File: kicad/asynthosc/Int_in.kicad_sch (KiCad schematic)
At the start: 7 parts, among them J7 AudioJack3, Q1 Q_NPN_BEC, SW2 SW_MEC_5G_LED

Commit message: bom: add jlcpcb field with simplified footprint
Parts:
- C33: JLC (none) -> 0603
- Q1: JLC (none) -> SOT-23
- R24, R25, R26: JLC (none) -> 0402
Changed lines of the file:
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@@
+			)
+		)
+		(property "JLC" ""
+			(at 118.11 60.96 0)
+			(effects
+				(font
+					(size 1.27 1.27)
+				)
+				(hide yes)
 			)
 		)
@@
 			)
 		)
+		(property "JLC" ""
+			(at 50.8 68.58 0)
+			(effects
+				(font
+					(size 1.27 1.27)
+				)
+				(hide yes)
+			)
+		)
 		(pin "S"
 		)
@@
 		)
 		(property "RefNum" "_generic_"
+			(at 71.12 66.04 0)
+			(effects
+				(font
+					(size 1.27 1.27)
+				)
+				(hide yes)
+			)
+		)
+		(property "JLC" "0402"
 			(at 71.12 66.04 0)
 			(effects
@@
 			)
 		)
+		(property "JLC" "0402"
+			(at 102.87 64.77 0)
+			(effects
+				(font
+					(size 1.27 1.27)
+				)
+				(hide yes)
+			)
+		)
 		(pin "1"
 		)
@@
 			)
 		)
+		(property "JLC" "0603"
+			(at 104.14 44.45 0)
+			(effects
+				(font
+					(size 1.27 1.27)
+				)
+				(hide yes)
+			)
+		)
 		(pin "2"
 		)
@@
 			)
 		)
+		(property "JLC" "SOT-23"
+			(at 82.55 66.04 0)
+			(effects
+				(font
+					(size 1.27 1.27)
+				)
+				(hide yes)
+			)
+		)
 		(pin "1"
 		)
@@
 			(at 85.09 53.34 0)
 			(effects
+				(font
+					(size 1.27 1.27)
+				)
+				(hide yes)
+			)
+		)
+		(property "JLC" "0402"
+			(at 85.09 53.34 0)
+			(effects

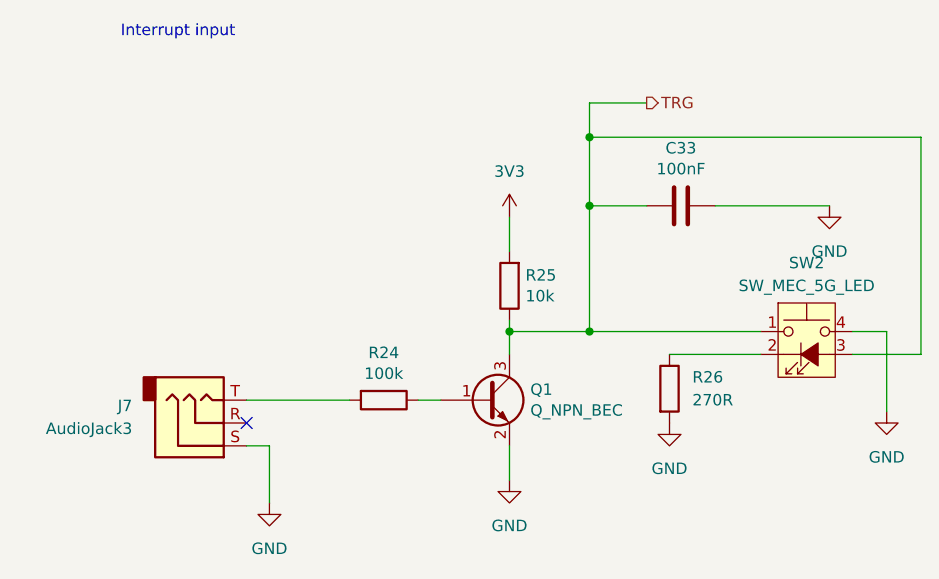
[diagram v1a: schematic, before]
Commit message: bom: dnp for all manually equiped components
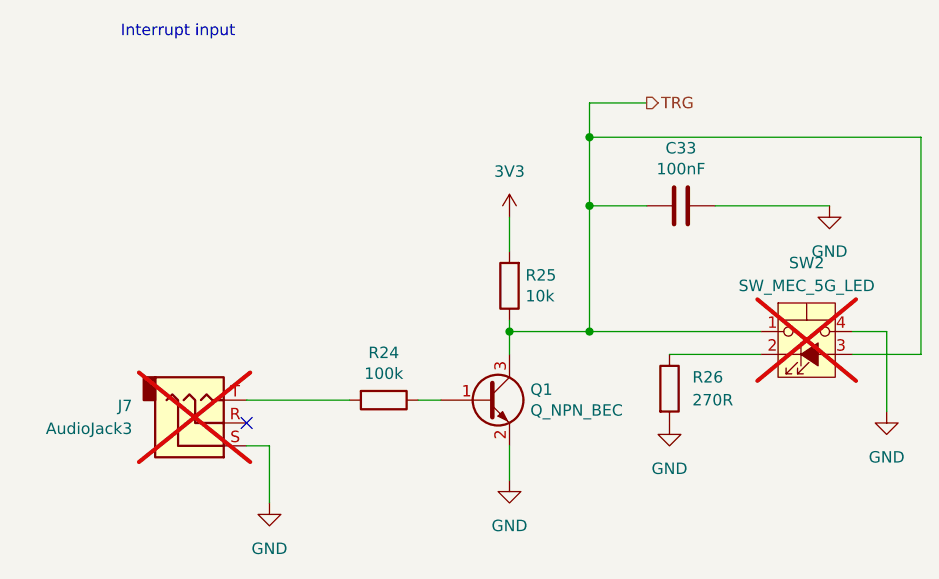
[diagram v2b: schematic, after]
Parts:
- J7, SW2: now not fitted
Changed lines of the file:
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@@
 		(in_bom yes)
 		(on_board yes)
-		(dnp no)
+		(dnp yes)
 		(fields_autoplaced yes)
 		(property "Reference" "SW2"
@@
 		(in_bom yes)
 		(on_board yes)
-		(dnp no)
+		(dnp yes)
 		(property "Reference" "J7"
 			(at 43.18 66.6749 0)

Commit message: bom: adding jlc ref to generic
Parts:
- C33: LCSC (none) -> C14663
- R24: LCSC (none) -> C25741
- R25: LCSC (none) -> C25744
- R26: LCSC (none) -> C144055
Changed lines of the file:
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@@
 			)
 		)
-		(property "LCSC" ""
+		(property "LCSC" "C25741"
 			(at 71.12 66.04 0)
 			(effects
@@
 			)
 		)
-		(property "LCSC" ""
+		(property "LCSC" "C144055"
 			(at 102.87 64.77 0)
 			(effects
@@
 			)
 		)
-		(property "LCSC" ""
+		(property "LCSC" "C14663"
 			(at 104.14 44.45 0)
 			(effects
@@
 			)
 		)
-		(property "LCSC" ""
+		(property "LCSC" "C25744"
 			(at 85.09 53.34 0)
 			(effects

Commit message: sch: update to k9 libs, fix nets
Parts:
- Q1: symbol Device:Q_NPN_BEC -> Transistor_BJT:Q_NPN_BEC
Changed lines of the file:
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@@
 	)
 	(symbol
-		(lib_id "Device:Q_NPN_BEC")
+		(lib_id "Transistor_BJT:Q_NPN_BEC")
 		(at 82.55 66.04 0)
 		(unit 1)
